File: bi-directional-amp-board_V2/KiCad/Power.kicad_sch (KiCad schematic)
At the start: 3 parts

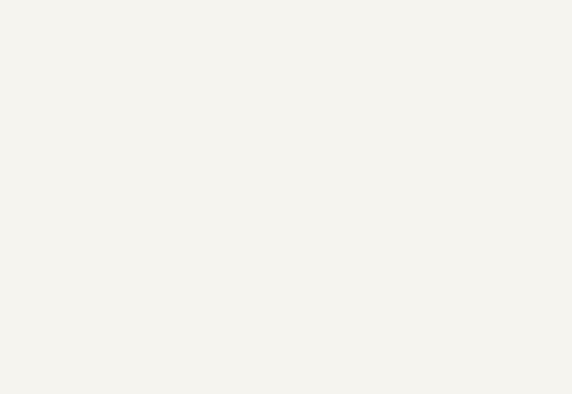
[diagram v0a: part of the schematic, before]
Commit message: re importing eagle files to kicad
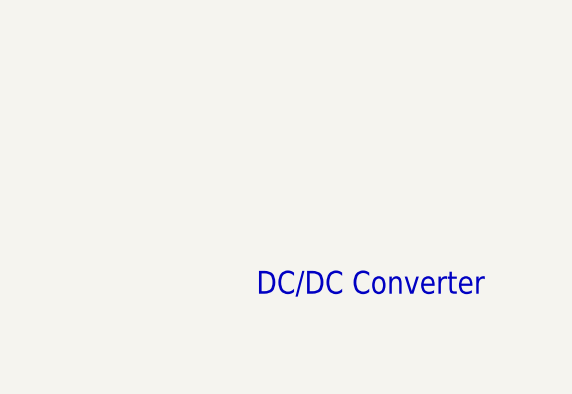
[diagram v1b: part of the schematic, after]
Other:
- note added: "DC/DC Converter"
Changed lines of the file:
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@@
 (kicad_sch (version 20211123) (generator eeschema)
-  (paper "User" 490.22 254.406)
+  (paper "A2")
   (junction (at 92.71 87.63) (diameter 0) (color 0 0 0 0)
   )
@@
     (effects (font (size 1.778 1.5113)) (justify left bottom))
   )
+  (text "DC/DC Converter" (at 208.28 205.74 180)
+    (effects (font (size 2.54 2.159)) (justify left bottom))
+  )
   (text "All passives size 0402 unless\notherwise noted" (at 31.75 213.36 180)

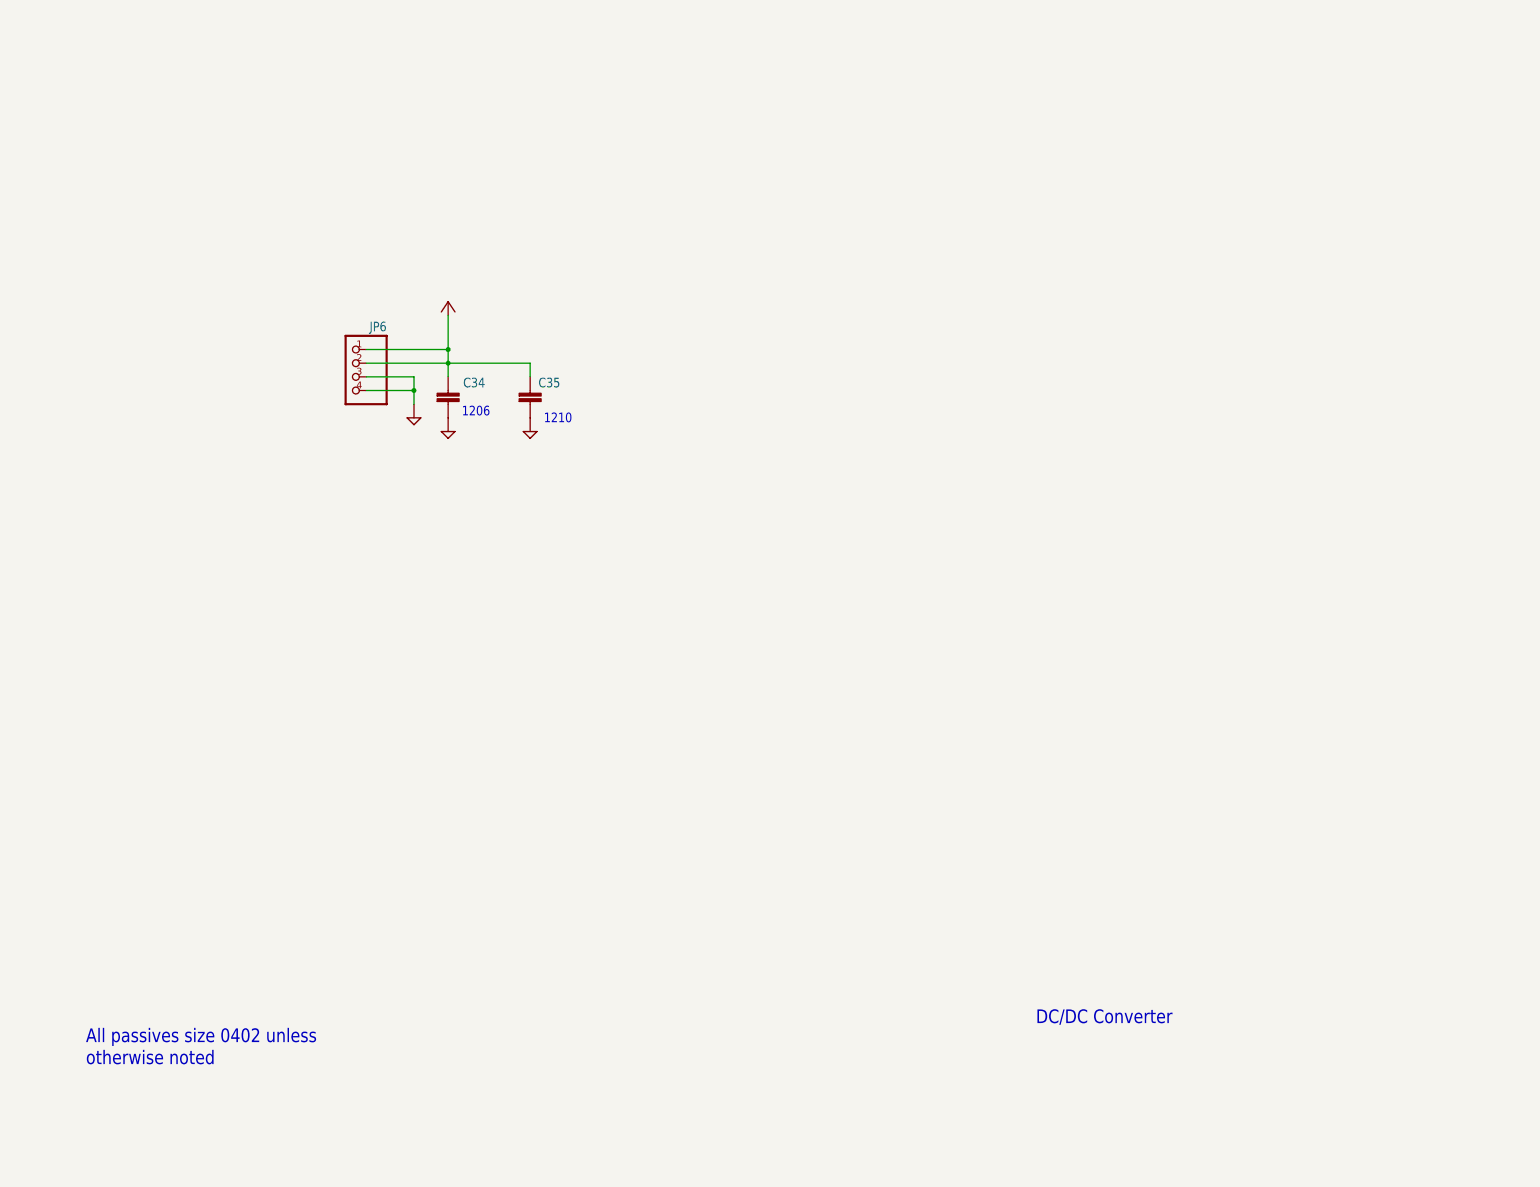
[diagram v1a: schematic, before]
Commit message: Updated KiCAD import of bidirectional amplifier. Still a bit broken, but better now.
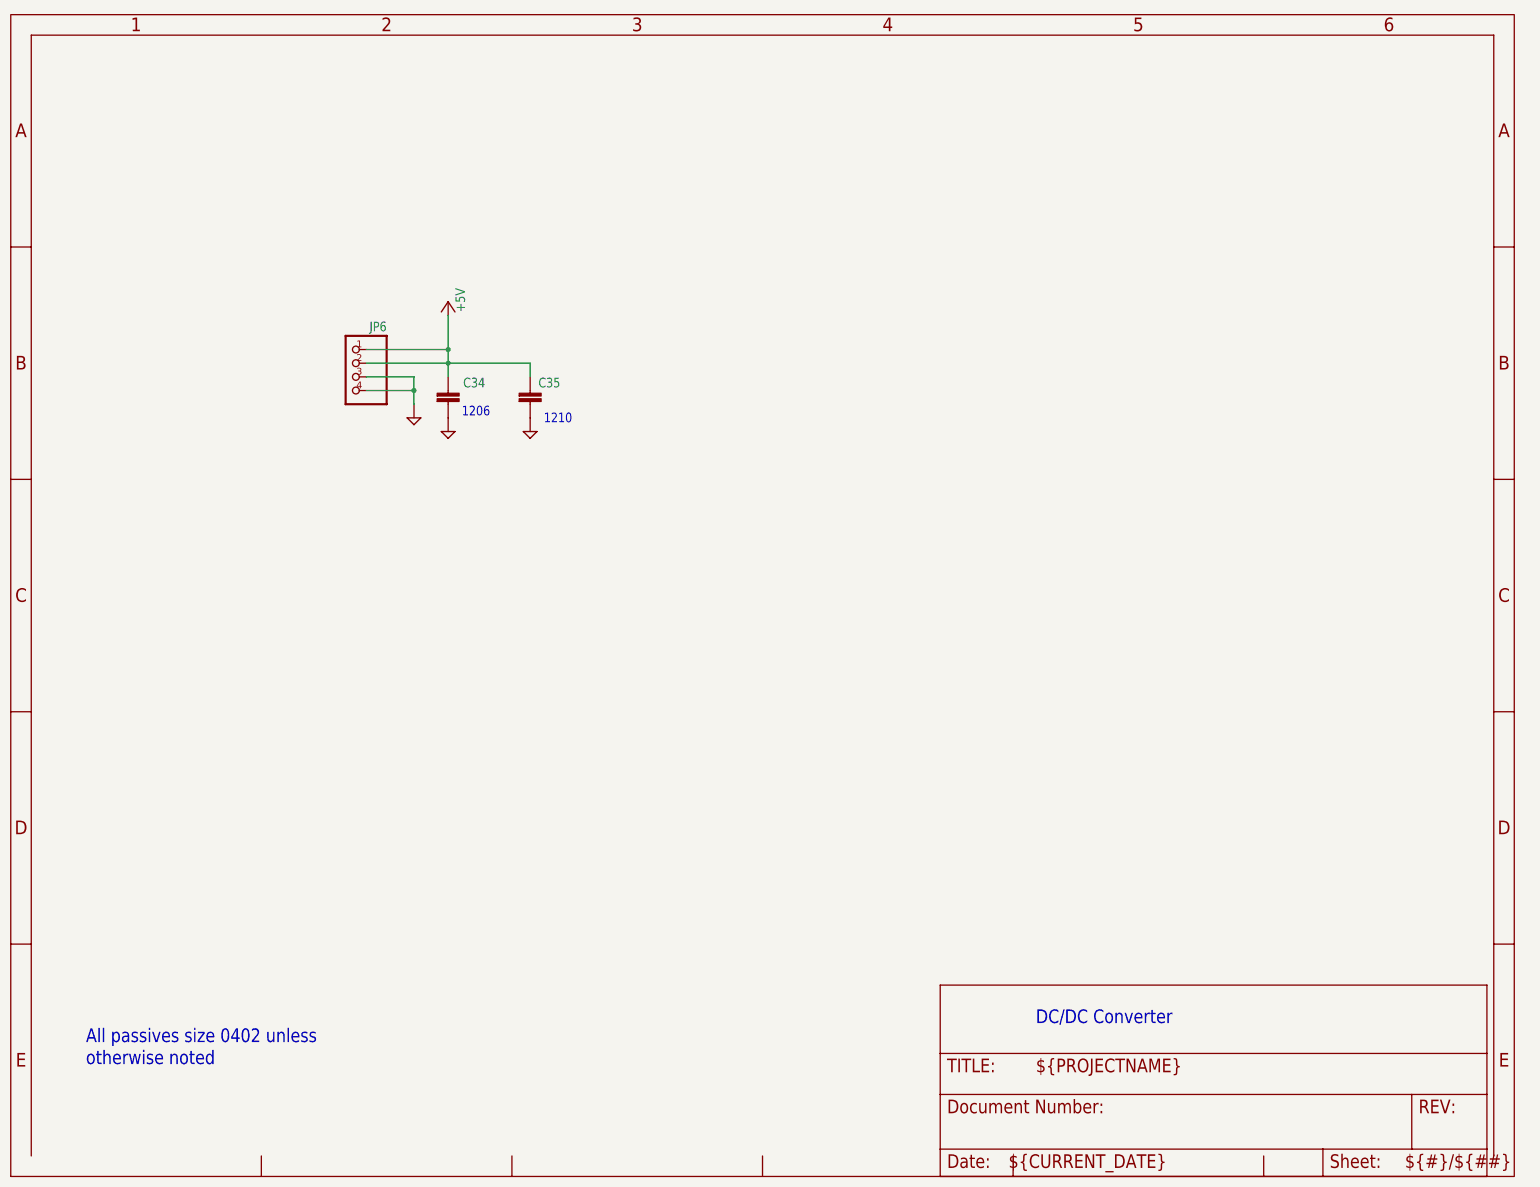
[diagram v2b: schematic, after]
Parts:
- C34: value (none) -> C-EUC1206; footprint (none) -> Bidirectional_Amp:C1206; MFR (none) -> Murata; MPN (none) -> GCJ31CR71C475KA01L; SIZE (none) -> 1206; VOLTAGE (none) -> 16V
- C35: value (none) -> C-EUC1210; footprint (none) -> Bidirectional_Amp:C1210; MFR (none) -> Murata; MPN (none) -> GCJ32ER71C226KE01L
- JP6: value (none) -> PINHD-1X4; footprint (none) -> Bidirectional_Amp:1X04
